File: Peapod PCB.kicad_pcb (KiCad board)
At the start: 2 copper layers, 72.5 x 29 mm, 24 parts, among them J1 CONN_01X01, J3 CONN_01X06, J5 CONN_01X01, J6 CONN_01X01, J7 CONN_01X02, U1 ESP8266

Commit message: making revisions to design
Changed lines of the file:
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@@
-(kicad_pcb (version 4) (host pcbnew 4.0.4-1.fc24-product)
+(kicad_pcb (version 4) (host pcbnew 4.0.5+dfsg1-4)
   (general
     (links 34)
     (no_connects 1)
-    (area 96.424999 71.924999 169.075001 101.075001)
+    (area 96.424999 30.163 223.01181 103.485733)
     (thickness 1.6002)
     (drawings 32)
-    (tracks 103)
+    (tracks 102)
     (zones 0)
     (modules 24)
@@
   )
   (setup
-    (last_trace_width 0.1524)
+    (last_trace_width 0.381)
     (user_trace_width 0.381)
     (user_trace_width 0.4)
@@
   (via (at 146 93.5) (size 0.6858) (drill 0.3302) (layers F.Cu B.Cu) (net 2))
   (via (at 126.65 99) (size 0.6858) (drill 0.3302) (layers F.Cu B.Cu) (net 2))
-  (segment (start 150 79.5) (end 147.962589 81.537411) (width 0.635) (layer F.Cu) (net 3))
-  (segment (start 147.962589 81.537411) (end 123.462589 81.537411) (width 0.635) (layer F.Cu) (net 3))
+  (segment (start 150 79.5) (end 147.88 81.62) (width 0.635) (layer F.Cu) (net 3))
+  (segment (start 147.8 81.625) (end 123.462589 81.625) (width 0.635) (layer F.Cu) (net 3))
   (segment (start 123.462589 81.537411) (end 122.275 82.725) (width 0.635) (layer F.Cu) (net 3))
   (segment (start 122.25 82.8) (end 122.25 84.185) (width 0.635) (layer F.Cu) (net 3))
@@
   (segment (start 101.5 94.365) (end 105.615 90.25) (width 0.635) (layer F.Cu) (net 10))
   (segment (start 101.5 97.5) (end 101.5 94.365) (width 0.635) (layer F.Cu) (net 10))
+  (segment (start 108 97.5) (end 108 94.365) (width 0.635) (layer F.Cu) (net 11))
+  (segment (start 108 94.365) (end 111.235 91.13) (width 0.635) (layer F.Cu) (net 11))
+  (segment (start 111.235 91.13) (end 128.726255 91.13) (width 0.635) (layer F.Cu) (net 11))
   (segment (start 154 93.136433) (end 154 93.5) (width 0.635) (layer F.Cu) (net 11))
   (segment (start 152.076156 91.212589) (end 154 93.136433) (width 0.635) (layer F.Cu) (net 11))
-  (segment (start 128.808844 91.212589) (end 152.076156 91.212589) (width 0.635) (layer F.Cu) (net 11))
-  (segment (start 128.771433 91.25) (end 128.808844 91.212589) (width 0.635) (layer F.Cu) (net 11))
-  (segment (start 111.115 91.25) (end 128.771433 91.25) (width 0.635) (layer F.Cu) (net 11))
-  (segment (start 108 97.5) (end 108 94.365) (width 0.635) (layer F.Cu) (net 11))
-  (segment (start 108 94.365) (end 111.115 91.25) (width 0.635) (layer F.Cu) (net 11))
+  (segment (start 128.808844 91.125) (end 152.076156 91.125) (width 0.635) (layer F.Cu) (net 11))
+  (segment (start 129.135 92) (end 151.75 92) (width 0.635) (layer F.Cu) (net 12))
   (segment (start 120.5 97.5) (end 123.635 97.5) (width 0.635) (layer F.Cu) (net 12))
   (segment (start 123.635 97.5) (end 129.135 92) (width 0.635) (layer F.Cu) (net 12))
-  (segment (start 129.135 92) (end 151.75 92) (width 0.635) (layer F.Cu) (net 12))
   (segment (start 151.75 92) (end 152 92.25) (width 0.635) (layer F.Cu) (net 12))
   (segment (start 152 92.25) (end 152 93.5) (width 0.635) (layer F.Cu) (net 12))

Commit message: final touches on peapod. Feature complete.
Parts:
- removed the G*** at (129.2, 91.2)
- removed the G*** at (129.2, 86.5)
- removed the G*** at (129.2, 81.8)
- removed the G*** at (119.0, 88.8)
- removed the G*** at (119.0, 84.0)
- removed the G*** at (109.0, 86.5)
- removed J5, J6: CONN_01X01, mod:Alligator Pad
- removed J7: CONN_01X02, mod:Bridge Pad
- removed R4, R5: 10k, Resistors_SMD:R_0805_HandSoldering
- removed REF**: 18650_outline, 18650_outline
- added FTDI: CONN_01X08, Pin_Headers:Pin_Header_Straight_1x08_Pitch2.54mm, F.Cu at (148.0, 98.5)
- added G***: LOGO, mod:star_1, F.Cu at (129.5, 96.2)
- added G***: LOGO, mod:star_1, F.Cu at (129.5, 91.8)
- added G***: LOGO, mod:star_1, F.Cu at (129.5, 94.0)
- added G***: LOGO, mod:star_1, F.Cu at (129.5, 79.2)
- added G***: LOGO, mod:star_1, F.Cu at (129.5, 85.5)
- added G***: LOGO, mod:star_1, F.Cu at (129.5, 88.0)
- added J2: CONN_01X01, mod:Alligator Pad, B.Cu at (159.5, 86.5)
- J1: moved to B.Cu
- J3: value CONN_01X06 -> CONN_01X01; footprint Pin_Headers:Pin_Header_Straight_1x06_Pitch2.54mm -> mod:Alligator Pad; moved to B.Cu
- moved J1 28.9 mm to (147.2, 86.5)
- moved R2 23.8 mm to (157.8, 74.0)
- moved R1 23.5 mm to (151.5, 74.0)
- moved BTN3 20.8 mm to (133.2, 79.2), turned to 90 degrees
- moved BT1 15.4 mm to (95.0, 87.2), turned to 90 degrees
- moved J3 12.0 mm to (153.5, 86.5), turned to 0 degrees
- moved R3 9.92 mm to (142.2, 93.5), turned to 90 degrees
- moved BTN1 9.25 mm to (133.2, 86.8), turned to 90 degrees
- moved G*** 9.25 mm to (112.8, 86.0)
- moved BTN2 7.57 mm to (133.2, 94.0), turned to 90 degrees
- moved G*** 4.04 mm to (105.0, 86.2)
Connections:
- J3 pad 1: GND -> Net-(J3-Pad1)
- R3 pad 1: +3V3 -> GPIO0
- R3 pad 2: Net-(R3-Pad2) -> +3V3
- U1 pad 10: Net-(R5-Pad1) -> GND
- U1 pad 11: Net-(R3-Pad2) -> +3V3
- U1 pad 12: Net-(J7-Pad1) -> GPIO0
- U1 pad 13: Net-(J6-Pad1) -> Net-(J3-Pad1)
- U1 pad 15: Net-(J3-Pad4) -> Net-(P1-Pad6)
- U1 pad 16: Net-(J3-Pad5) -> Net-(P1-Pad7)
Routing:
- net Net-(J2-Pad1): track 61.0 -> 8.45 mm, vias 0 -> 1
- net Net-(J6-Pad1): track 51.6 -> 0.00 mm
- net Net-(J7-Pad1): track 41.7 -> 0.00 mm
- net Net-(R1-Pad1): track 32.4 -> 9.71 mm
- net Net-(BTN3-Pad2): track 43.4 -> 20.8 mm
- net Net-(R5-Pad1): track 22.4 -> 0.00 mm
- net Net-(R3-Pad2): track 18.3 -> 0.00 mm
- net GPIO0: track 0.00 -> 17.7 mm
- net +3V3: track 125.1 -> 140.1 mm
- net Net-(BTN1-Pad2): track 34.9 -> 21.7 mm
- net Net-(J3-Pad1): track 0.00 -> 7.26 mm, vias 0 -> 1
- net Net-(J1-Pad1): track 6.87 -> 13.8 mm, vias 0 -> 1
- net GND: track 13.4 -> 19.9 mm, vias 12 -> 7
- net Net-(P1-Pad7): track 0.00 -> 6.47 mm
- net Net-(J3-Pad5): track 6.31 -> 0.00 mm
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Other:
- board size 72.5 x 29 mm -> 77.5 x 29 mm
- net class Signal added: clearance 0.3048, trace_width 0.6858, via_dia 0.6858, via_drill 0.3302
- board text added: "3v3"
- board text added: "R3"
- board text added: "Rx"
- board text added: "Tx"

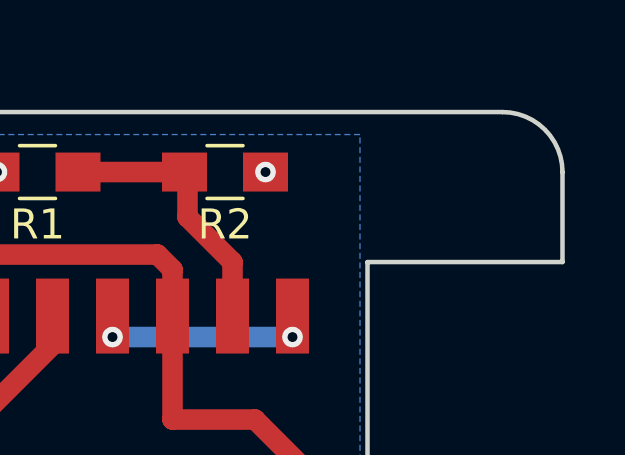
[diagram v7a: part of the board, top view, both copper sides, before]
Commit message: added a keychain(?) hole, created gerbers and BOM file.
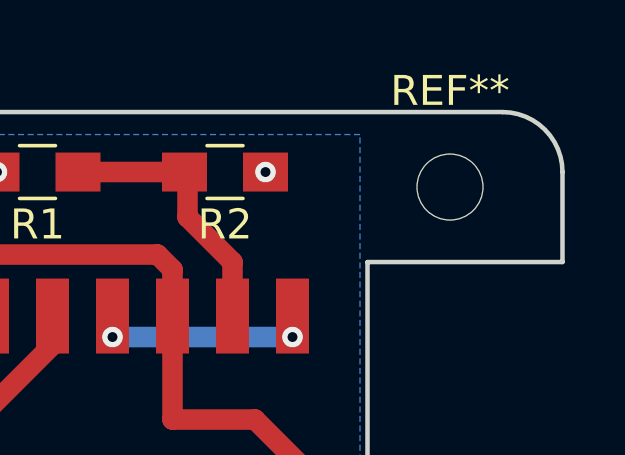
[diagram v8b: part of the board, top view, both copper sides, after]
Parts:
- added REF**: MountingHole_2.2mm_M2, Mounting_Holes:MountingHole_2.2mm_M2, F.Cu at (165.2, 74.5)
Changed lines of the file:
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@@
     (tracks 103)
     (zones 0)
-    (modules 20)
+    (modules 21)
     (nets 16)
   )
@@
       (xy 0.005871 -0.739191) (xy 0.006395 -0.740741) (xy 0.006479 -0.740964) (xy 0.006894 -0.740455)) (layer F.SilkS) (width 0.01))
   )
+  (module Mounting_Holes:MountingHole_2.2mm_M2 (layer F.Cu)
+    (at 165.25 74.5)
+    (descr "Mounting Hole 2.2mm, no annular, M2")
+    (tags "mounting hole 2.2mm no annular m2")
+    (fp_text reference REF** (at 0 -3.2) (layer F.SilkS)
+      (effects (font (size 1 1) (thickness 0.15)))
+    )
+    (fp_text value MountingHole_2.2mm_M2 (at 0 3.2) (layer F.Fab)
+      (effects (font (size 1 1) (thickness 0.15)))
+    )
+    (fp_circle (center 0 0) (end 2.2 0) (layer Cmts.User) (width 0.15))
+    (fp_circle (center 0 0) (end 2.45 0) (layer F.CrtYd) (width 0.05))
+    (pad 1 np_thru_hole circle (at 0 0) (size 2.2 2.2) (drill 2.2) (layers *.Cu *.Mask))
+  )
   (dimension 29 (width 0.3) (layer Dwgs.User)
